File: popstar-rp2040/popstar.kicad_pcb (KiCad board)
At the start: 2 copper layers, 182 parts, among them J1 JST SH 4-pin, J2 SWD, SW1 Boot, SW10 MX_SW_solder, SW11 MX_SW_solder, SW12 MX_SW_solder, SW13 MX_SW_solder, SW14 MX_SW_solder, SW15 MX_SW_solder, SW16 MX_SW_solder, SW17 MX_SW_solder, SW18 MX_SW_solder, SW19 MX_SW_solder, SW2 MX_SW_solder, SW20 MX_SW_solder, SW21 MX_SW_solder, SW22 MX_SW_solder, SW23 MX_SW_solder, SW24 MX_SW_solder, SW25 MX_SW_solder, SW26 MX_SW_solder, SW27 MX_SW_solder, SW28 MX_SW_solder, SW29 MX_SW_solder, SW3 MX_SW_solder, SW30 MX_SW_solder, SW31 MX_SW_solder, SW32 MX_SW_solder, SW33 MX_SW_solder, SW34 MX_SW_solder, SW35 MX_SW_solder, SW36 MX_SW_solder, SW37 MX_SW_solder, SW38 MX_SW_solder, SW39 MX_SW_solder, SW4 MX_SW_solder, SW40 MX_SW_solder, SW41 MX_SW_solder, SW42 MX_SW_solder, SW43 MX_SW_solder, SW44 MX_SW_solder, SW45 MX_SW_solder, SW46 MX_SW_solder, SW47 MX_SW_solder, SW48 MX_SW_solder, SW49 MX_SW_solder, SW5 MX_SW_solder, SW50 MX_SW_solder, SW51 MX_SW_solder, SW52 MX_SW_solder, SW53 MX_SW_solder, SW54 MX_SW_solder, SW55 MX_SW_solder, SW56 MX_SW_solder, SW57 MX_SW_solder, SW58 MX_SW_solder, SW59 MX_SW_solder, SW6 MX_SW_solder, SW60 MX_SW_solder, SW61 MX_SW_solder, SW62 MX_SW_solder, SW7 MX_SW_solder, SW8 MX_SW_solder, SW9 MX_SW_solder, U2 XC6206PxxxMR, U3 SRV05-4, U4 W25Q128JVS, U5 74AHCT1G125, U6 RP2040, Y1 12MHz

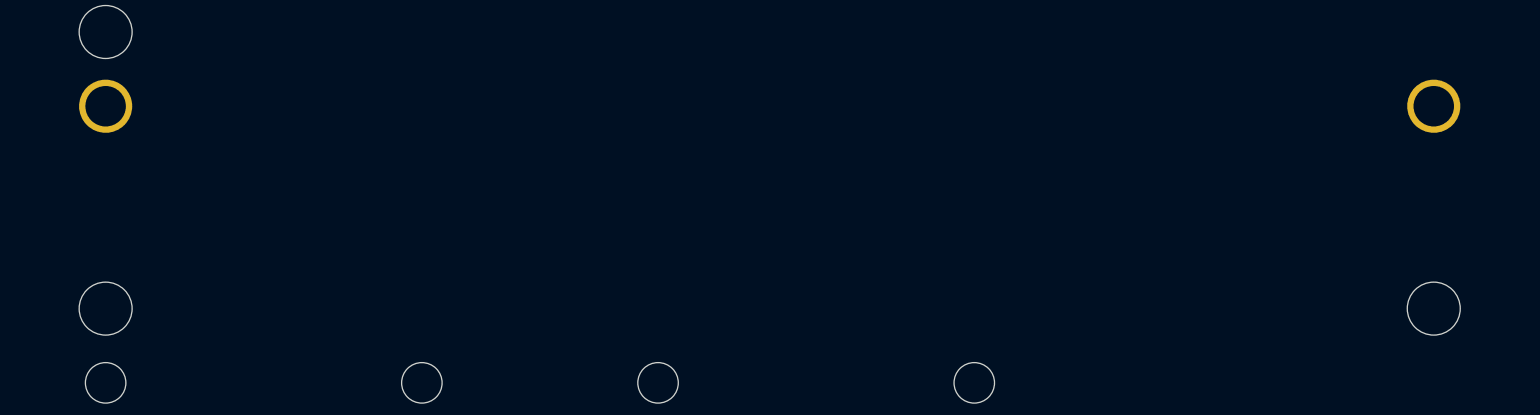
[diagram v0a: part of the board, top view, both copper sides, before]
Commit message: Correct 2.25 left shift to use 2.25 stab footprint
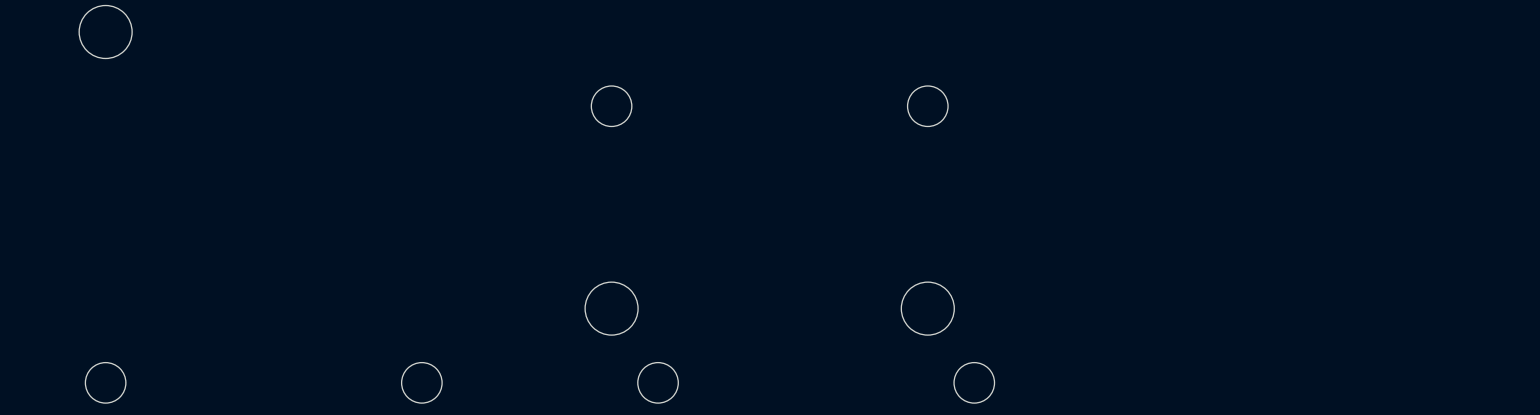
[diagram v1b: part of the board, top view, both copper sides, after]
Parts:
- S4: footprint marbastlib-mx:STAB_MX_P_6.25u -> marbastlib-mx:STAB_MX_2.25u

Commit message: Placed switch, stabs, and diode components in the proper places.
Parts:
- D13, D14, D15, D16, D17, D18, D19, D20, D21, D22, D23, D24, D25, D26, D27, D28, D29, D30, D31, D32, D33, D34, D35, D36, D37, D38, D39, D40, D41, D42, D43, D44, D45, D46, D47, D48, D49, D50, D51, D52, D53, D54, D55, D56, D57, D58, D59, D60, D61, D62, D63, D64, D65, D66, D67, D68, D69, D70, D71: moved to B.Cu
- moved S2 298.2 mm to (296.1, 79.4)
- moved S1 288.5 mm to (298.4, 41.3)
- moved C10 288.3 mm to (471.9, 2.88)
- moved C11 288.3 mm to (471.9, 4.85)
- moved C12 288.3 mm to (471.9, 6.82)
- moved C13 288.3 mm to (474.8, -3.03)
- moved C14 288.3 mm to (474.8, -1.06)
- moved C15 288.3 mm to (474.8, 0.91)
- moved C16 288.3 mm to (474.8, 2.88)
- moved C17 288.3 mm to (474.8, 4.85)
- moved C28 288.3 mm to (433.4, 161.3)
- moved C29 288.3 mm to (433.4, 163.3)
- moved C30 288.3 mm to (433.4, 165.2)
- moved C7 288.3 mm to (471.9, -3.03)
- moved C8 288.3 mm to (471.9, -1.06)
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
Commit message: Placed crystal oscillator components in the proper places.
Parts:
- C13, C14, R4, U6, Y1: moved to B.Cu
- moved C14 427.9 mm to (55.6, 84.9), turned to 90 degrees
- moved R4 425.0 mm to (57.9, 80.7), turned to 90 degrees
- moved C13 421.3 mm to (62.7, 84.9), turned to -90 degrees
- moved U6 416.9 mm to (59.5, 71.4), turned to 135 degrees
- moved Y1 416.2 mm to (59.0, 84.1)

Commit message: Added edge cuts, front silkscreen, adjusted diodes to not interfere with edge cuts
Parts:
- D72: moved to B.Cu
- moved D72 20.6 mm to (290.5, 62.7)
- moved D65 16.7 mm to (299.2, 100.8)
- moved D1 0.47 mm to (69.8, 113.2)
- moved D10 0.47 mm to (276.2, 123.5)
- moved D11 0.47 mm to (273.8, 117.2)
- moved D12 0.47 mm to (279.4, 118.7)
- moved D2 0.47 mm to (64.3, 117.2)
- moved D3 0.47 mm to (66.7, 123.5)
- moved D4 0.47 mm to (73.0, 123.5)
- moved D5 0.47 mm to (75.4, 117.2)
- moved D6 0.47 mm to (69.8, 118.7)
- moved D7 0.47 mm to (279.4, 113.2)
- moved D8 0.47 mm to (285.0, 117.2)
- moved D9 0.47 mm to (282.6, 123.5)
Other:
- board outline added: 284.7 x 94.2 mm

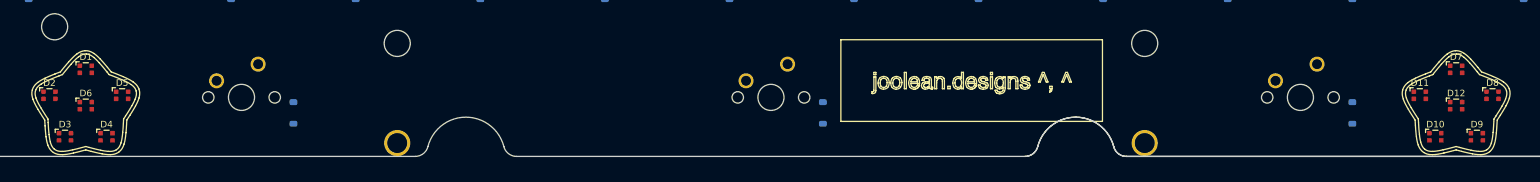
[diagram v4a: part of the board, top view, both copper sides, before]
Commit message: Removed silkscreen near MCU + silkscreen collision with star LEDs
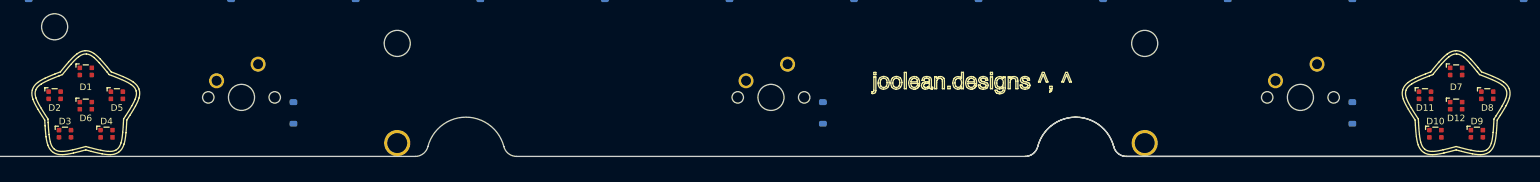
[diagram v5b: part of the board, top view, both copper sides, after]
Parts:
- moved D2 0.79 mm to (65.1, 117.2)
- moved D5 0.79 mm to (74.6, 117.2)
- moved D11 0.79 mm to (274.6, 117.2)
- moved D8 0.79 mm to (284.2, 117.2)
- moved D10 0.47 mm to (276.2, 123.0)
- moved D3 0.47 mm to (66.7, 123.0)
- moved D4 0.47 mm to (73.0, 123.0)
- moved D9 0.47 mm to (282.6, 123.0)
- moved D1 0.32 mm to (69.8, 113.5)
- moved D7 0.32 mm to (279.4, 113.5)

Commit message: Added more decoupling capacitors near MCU, debug, cleaned up component positioning a bit
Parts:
- C1, C10, C11, C17, C2, C3, C4, C5, C6, C7, C8, C9, J2, R5, SW1, U4: moved to B.Cu
- moved C12 485.6 mm to (-10.2, 65.1)
- moved C15 485.6 mm to (-7.33, 59.1)
- moved C16 485.6 mm to (-7.33, 61.1)
- moved F1 485.6 mm to (0.50, 75.3)
- moved R1 485.6 mm to (-3.76, 74.7)
- moved R2 485.6 mm to (-7.25, 76.6)
- moved R3 485.6 mm to (-7.25, 79.1)
- moved J1 485.6 mm to (-0.79, 69.8)
- moved U2 485.6 mm to (1.91, 63.2)
- moved U3 485.6 mm to (-3.24, 63.2)
- moved J2 432.5 mm to (38.9, 70.6), turned to -90 degrees
- moved C8 424.5 mm to (53.2, 69.1), turned to 90 degrees
- moved C9 423.2 mm to (55.5, 76.5), turned to -90 degrees
- moved C3 421.6 mm to (54.2, 76.5), turned to -90 degrees
- moved C10 417.2 mm to (59.2, 64.0), turned to 90 degrees
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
